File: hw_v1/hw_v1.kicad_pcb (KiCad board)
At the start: 4 copper layers, 116.5 x 98 mm, 234 parts, among them J10 Conn_01x01, J11 Conn_01x01, J12 Delphi_Sicma_24, J13 Delphi_Sicma_24, J14 Conn_01x04, J2 Conn_01x05, J3 Conn_01x05, J4 Conn_01x05, J5 Conn_01x03, J6 Conn_01x04, J8 USB_B, J9 Tag connect, Q1 AO3400A, Q2 AO3400A, Q3 FDS6890A, Q5 SS8050, Q6 AO3400A, SW2 SW_Push, U1 MCZ33810EK, U10 BMP280, U11 L78M05ABDT-TR, U12 LM74800, U13 STM32F407VGTx, U14 TJA1051T-3, U15 25LCxxx, U16 REF3033, U17 SRV05-4, U18 VNLD5090, U19 L78M05ABDT-TR, U2 TC4424A, U21 ADXL343, U3 TC4424A, U4 MAX9926UAEE+, U5 TPL7407LAPWR, U6 LMV324, U7 LMV324, U9 SP720ABTG, Y1 32.768kHz, Y2 25MHz

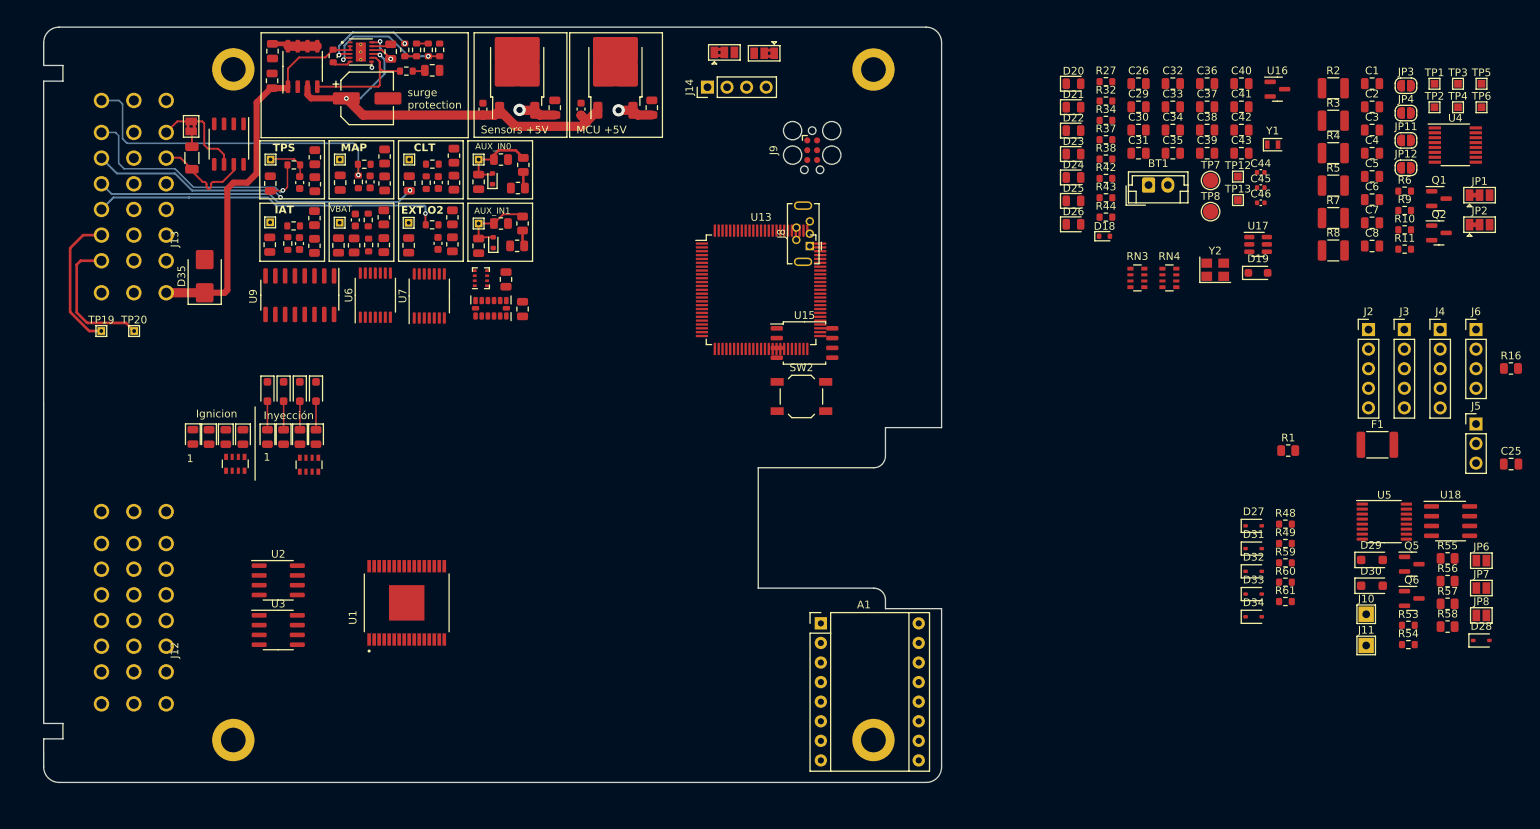
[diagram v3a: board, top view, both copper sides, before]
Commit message: placed al SMD, wip pmic traces
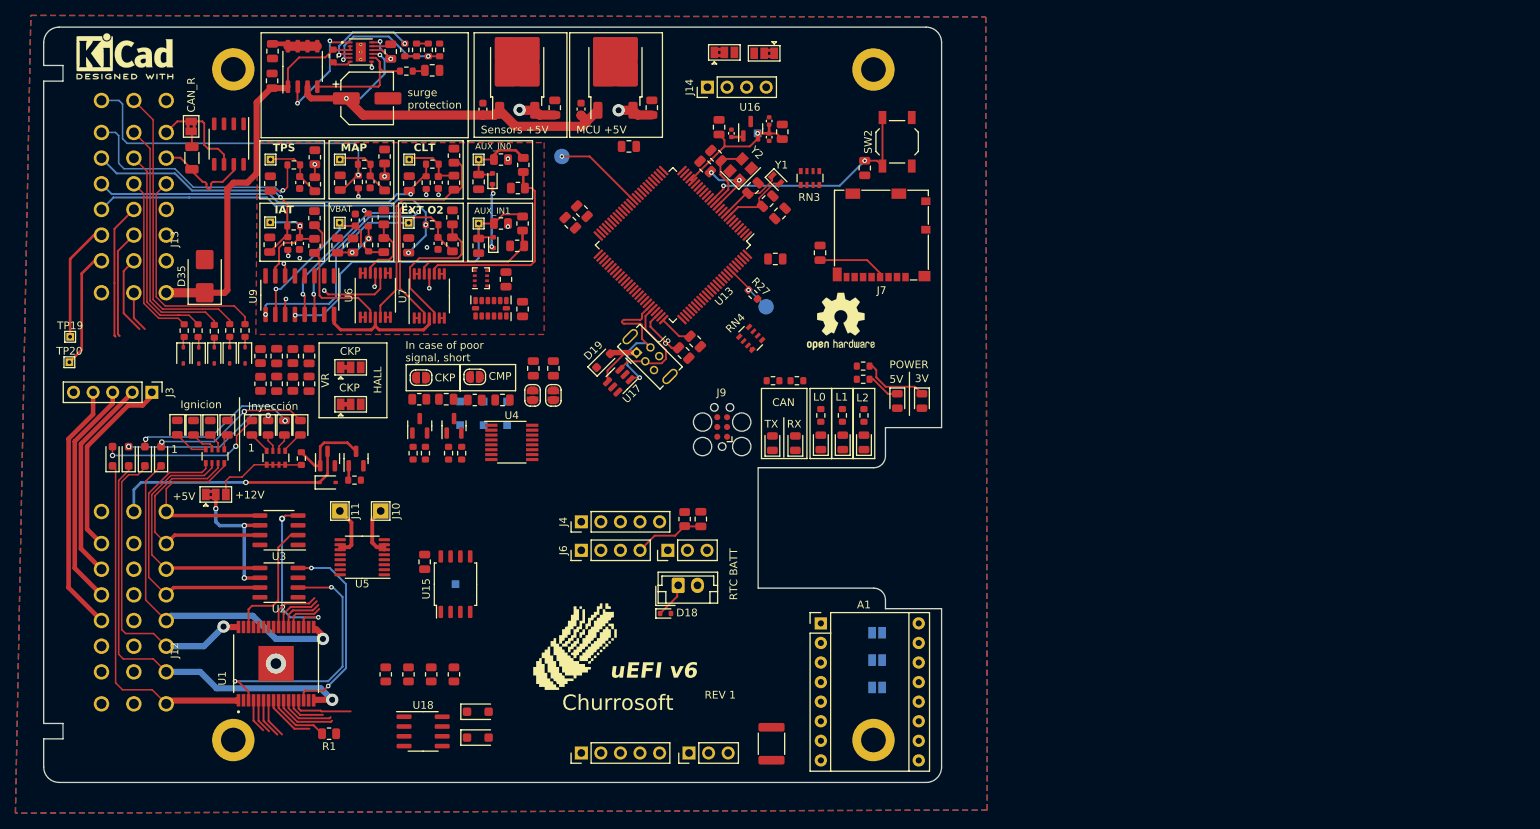
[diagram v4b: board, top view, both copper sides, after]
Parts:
- added Churrosoft: SYM_Hot_Large, OpenEFI-STM32F_rev3:churro_new_v4, F.Cu at (119.1, 133.7)
- added G***: LOGO, LOGO, B.Cu at (100.5, 102.0)
- added J15: Conn_01x03, Connector_PinHeader_2.54mm:PinHeader_1x03_P2.54mm_Vertical, F.Cu at (133.7, 147.5)
- added J7: 104031-0811, Connector_Card:microSD_HC_Molex_104031-0811, F.Cu at (158.7, 80.3)
- added JP13: Jumper_3_Bridged12, Jumper:SolderJumper-3_P1.3mm_Bridged2Bar12_Pad1.0x1.5mm, F.Cu at (72.3, 114.0)
- added LOGO1: Logo_Open_Hardware_Large, Symbol:OSHW-Logo2_9.8x8mm_SilkScreen, F.Cu at (153.4, 91.5)
- added SYM1: SYM_Hot_Small, Symbol:KiCad-Logo2_5mm_SilkScreen, F.Cu at (60.5, 57.1)
- JP6, JP7, JP8, TP1, TP12, TP13, TP2, TP3, TP4, TP5, TP6, TP7, TP8: moved to B.Cu
- R2, R3, R4, R5, R7, R8: footprint Resistor_SMD:R_1210_3225Metric -> Resistor_SMD:R_0805_2012Metric
- moved J3 162.7 mm to (64.0, 100.7), turned to -90 degrees
- moved D28 151.1 mm to (86.8, 112.4)
- moved JP2 148.3 mm to (89.8, 102.3)
- moved JP1 148.2 mm to (89.8, 97.5)
- moved C3 145.9 mm to (80.2, 99.6), turned to 90 degrees
- moved C2 145.8 mm to (80.2, 96.0), turned to -90 degrees
- moved R54 145.6 mm to (83.4, 109.3), turned to 90 degrees
- moved R49 145.5 mm to (68.2, 92.7), turned to 90 degrees
- moved R59 144.3 mm to (70.0, 92.7), turned to 90 degrees
- moved R2 143.5 mm to (78.1, 96.0), turned to -90 degrees
- moved C1 143.3 mm to (84.4, 99.6), turned to 90 degrees
- moved R60 142.7 mm to (72.1, 92.8), turned to 90 degrees
- moved Q6 141.8 mm to (86.8, 109.3), turned to 90 degrees
- moved R5 141.6 mm to (78.1, 99.6), turned to 90 degrees
- moved R61 141.4 mm to (74.1, 92.7), turned to 90 degrees
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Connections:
- A1 pad 15: /Relay & Power Outputs/MTR_STEP -> /MTR_STEP
- A1 pad 16: /Relay & Power Outputs/MTR_DIR -> /MTR_DIR
- A1 pad 2: /Relay & Power Outputs/MTR_FAULT -> /MTR_FAULT
- A1 pad 9: /Relay & Power Outputs/MTR_ENABLE -> /MTR_ENABLE
- C2 pad 1: CKP- -> CRANK-
- C3 pad 1: CMP- -> CAM-
- C7 pad 1: /CKP_CMP_Sensors/CKP -> /CKP
- C8 pad 1: /CKP_CMP_Sensors/CKP -> /CKP
- D27 pad 1: /Connector/SW_Clutch_m -> /SW_Clutch_m
- D31 pad 1: /Connector/SW_USER_m -> /SW_USER_m
- D32 pad 1: /Connector/SW_TABLE_m -> /SW_TABLE_m
- D33 pad 1: /Connector/SW_SHIFT_m -> /SW_SHIFT_m
- D34 pad 1: /Connector/SW_AC_m -> /SW_AC_m
- JP1 pad 2: CMP+ -> CAM+
- JP2 pad 2: CKP+ -> CRANK+
- Q1 pad 2: /CKP_CMP_Sensors/CMP -> /CMP
- Q2 pad 2: /CKP_CMP_Sensors/CKP -> /CKP
- R1 pad 2: /Injection & ignition drivers/PMIC1_ENABLE -> /PMIC1_ENABLE
- R10 pad 2: /CKP_CMP_Sensors/CMP -> /CMP
- R11 pad 2: /CKP_CMP_Sensors/CKP -> /CKP
- R2 pad 1: CKP- -> CRANK-
- R48 pad 1: /Connector/SW_Clutch_m -> /SW_Clutch_m
- R49 pad 1: /Connector/SW_USER_m -> /SW_USER_m
- R5 pad 1: CMP- -> CAM-
- R53 pad 1: /Relay & Power Outputs/RPM_OUT -> /RPM_OUT
- R55 pad 1: /Relay & Power Outputs/idle -> /idle
- R56 pad 2: /Relay & Power Outputs/boost -> /boost
- R57 pad 2: /Relay & Power Outputs/idle -> /idle
- R58 pad 2: /Relay & Power Outputs/boost -> /boost
- R59 pad 1: /Connector/SW_TABLE_m -> /SW_TABLE_m
- R6 pad 2: /CKP_CMP_Sensors/CMP -> /CMP
- R60 pad 1: /Connector/SW_SHIFT_m -> /SW_SHIFT_m
- R61 pad 1: /Connector/SW_AC_m -> /SW_AC_m
- R9 pad 2: /CKP_CMP_Sensors/CKP -> /CKP
- TP5 pad 1: /CKP_CMP_Sensors/CKP -> /CKP
- TP6 pad 1: /CKP_CMP_Sensors/CMP -> /CMP
- U1 pad 10: /Injection & ignition drivers/INY1 -> /INY1
- U1 pad 11: /Injection & ignition drivers/INY2 -> /INY2
- U1 pad 12: /Injection & ignition drivers/INY3 -> /INY3
- U1 pad 13: /Injection & ignition drivers/INY4 -> /INY4
- U1 pad 21: /Injection & ignition drivers/ECN4 -> /ECN3
- U1 pad 22: /Injection & ignition drivers/ECN3 -> /ECN4
- U1 pad 23: /Injection & ignition drivers/ECN2 -> /ECN1
- U1 pad 24: /Injection & ignition drivers/ECN1 -> /ECN2
- U1 pad 4: /Injection & ignition drivers/PMIC1_CS -> /PMIC1_CS
- U1 pad 5: /Injection & ignition drivers/SPI2_SCK -> /SPI2_SCK
- U1 pad 6: /Injection & ignition drivers/SPI2_MOSI -> /SPI2_MOSI
- U1 pad 7: /Injection & ignition drivers/SPI2_MISO -> /SPI2_MISO
- U1 pad 9: /Injection & ignition drivers/PMIC1_ENABLE -> /PMIC1_ENABLE
- U10 pad 2: /Sensors/BARO_CS -> /ACCL_CS
- U10 pad 3: /Sensors/SPI2_MOSI -> /SPI2_MOSI
- U10 pad 4: /Sensors/SPI2_SCK -> /SPI2_SCK
- U10 pad 5: /Sensors/SPI2_MISO -> /SPI2_MISO
- U13 pad 23: /TPS -> /IAT
- U13 pad 34: /BARO_CS -> /ACCL_CS
- U21 pad 12: /Sensors/SPI2_MISO -> /SPI2_MISO
- U21 pad 13: /Sensors/SPI2_MOSI -> /SPI2_MOSI
- U21 pad 14: /Sensors/SPI2_SCK -> /SPI2_SCK
- U21 pad 7: /Sensors/ACCL_CS -> /ACCL_CS
- U4 pad 4: /CKP_CMP_Sensors/CMP -> /CMP
- U4 pad 5: /CKP_CMP_Sensors/CKP -> /CKP
- U5 pad 1: /Relay & Power Outputs/fuel_pump -> /fuel_pump
- U5 pad 2: /Relay & Power Outputs/fan1 -> /fan1
- U5 pad 3: /Relay & Power Outputs/fan2 -> /fan2
- U5 pad 4: /Relay & Power Outputs/vvt -> /vvt
- U5 pad 5: /Relay & Power Outputs/vvt -> /vvt
- U6 pad 1: /Sensors/IAT -> /IAT
- U6 pad 13: /Sensors/VBATT -> VBATT
- U6 pad 14: /Sensors/VBATT -> VBATT
- U6 pad 2: /Sensors/IAT -> /IAT
- U6 pad 6: /Sensors/CLT -> /CLT
- U6 pad 7: /Sensors/CLT -> /CLT
- U6 pad 8: /Sensors/TPS -> /TPS
- U6 pad 9: /Sensors/TPS -> /TPS
- U7 pad 1: /Sensors/MAP -> /MAP
- U7 pad 2: /Sensors/MAP -> /MAP
- U7 pad 6: /Sensors/O2 -> /O2
- U7 pad 7: /Sensors/O2 -> /O2
- U9 pad 1: /Sensors/AUX_CH5_m -> unconnected-(U9-I1-Pad1)
- U9 pad 12: /Sensors/AUX_CH6_m -> ext_a0_in
- U9 pad 13: /Sensors/AUX_CH8_m -> ext_a1_in
- U9 pad 2: /Sensors/AUX_CH3_m -> unconnected-(U9-I2-Pad2)
- U9 pad 3: /Sensors/AUX_CH2_m -> unconnected-(U9-I3-Pad3)
- U9 pad 4: /Sensors/AUX_CH1_m -> unconnected-(U9-I4-Pad4)
- U9 pad 5: /Sensors/AUX_CH4_m -> unconnected-(U9-I5-Pad5)
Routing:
- net +5C: track 4.85 -> 78.8 mm, vias 1 -> 6
- net INJ-2-OUT: track 0.00 -> 57.4 mm, vias 0 -> 1
- net INJ-4-OUT: track 0.00 -> 45.5 mm, vias 0 -> 1
- net INJ-1-OUT: track 0.00 -> 45.4 mm
- net INJ-3-OUT: track 0.00 -> 40.1 mm, vias 0 -> 1
- net PROTO-5: track 0.00 -> 40.0 mm
- net SW_AC: track 0.00 -> 38.4 mm
- net ext_a1_in: track 10.9 -> 48.9 mm, vias 0 -> 2
- net /Sensors/CH_CLT_m: track 0.00 -> 37.6 mm, vias 0 -> 2
- net +3V3: track 0.00 -> 36.7 mm
- net /Sensors/CH_O2_m: track 0.00 -> 36.2 mm, vias 0 -> 1
- net IGN-1-OUT: track 0.00 -> 36.1 mm
- net /Sensors/CH_MAP_m: track 0.00 -> 34.7 mm, vias 0 -> 1
- net Net-(U1-GD0): track 0.00 -> 33.5 mm, vias 0 -> 2
- net ext_a0_in: track 10.2 -> 43.5 mm, vias 0 -> 1
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- added copper zone on B.Cu, net GND
- added copper zone on F.Cu, net GND
- added copper zone on In1.Cu, net GND
- added copper zone on In2.Cu, net GND
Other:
- board text added: "+12V"
- board text added: "+5V"
- board text added: "3V"
- board text added: "5V"
- board text added: "CAN"
- board text added: "CAN_R"
- board text added: "CKP"
- board text added: "CMP"
- board text added: "HALL"
- board text added: "In case of poor signal, short"
- board text added: "L0"
- board text added: "L1"
- board text added: "L2"
- board text added: "POWER"
- board text added: "REV 1"
- board text added: "RTC BATT"
- board text added: "RX"
- board text added: "TX"
- board text added: "VR"
- board text added: "uEFI v6"

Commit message: ckp/cmp sensor layout
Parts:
- removed LOGO1: Logo_Open_Hardware_Large, Symbol:OSHW-Logo2_9.8x8mm_SilkScreen
- removed SYM1: SYM_Hot_Small, Symbol:KiCad-Logo2_5mm_SilkScreen
- moved TP1 32.5 mm to (78.1, 96.2)
- moved RN3 12.3 mm to (149.8, 85.2)
- moved TP5 5.57 mm to (106.0, 107.1)
- moved JP10 5.25 mm to (138.2, 56.8)
- moved JP9 4.82 mm to (143.1, 56.9)
- moved TP6 3.65 mm to (100.5, 106.0)
- moved TP3 3.65 mm to (105.3, 98.7)
- moved TP2 1.90 mm to (111.2, 103.4)
- moved TP4 1.47 mm to (106.8, 103.5)
- moved C35 0.90 mm to (150.7, 81.7)
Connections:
- J12 pad B7: FUELPUMP-OUT -> VVT-OUT
- J12 pad C2: VVT-OUT -> IDLE-OUT
- J12 pad C3: IDLE-OUT -> FUELPUMP-OUT
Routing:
- net /CAN1_RX: track 0.00 -> 83.0 mm, vias 0 -> 2
- net /CAN1_TX: track 0.00 -> 79.8 mm, vias 0 -> 2
- net /CKP_CMP_Sensors/IN1-: track 0.00 -> 47.8 mm, vias 0 -> 2
- net /CKP_CMP_Sensors/IN1+: track 0.00 -> 43.6 mm, vias 0 -> 3
- net /CKP_CMP_Sensors/IN2-: track 0.00 -> 43.1 mm, vias 0 -> 4
- net CRANK+: track 14.5 -> 53.0 mm
- net /CKP_CMP_Sensors/IN2+: track 0.00 -> 38.4 mm, vias 0 -> 3
- net FUELPUMP-OUT: track 0.00 -> 37.1 mm, vias 0 -> 1
- net CAM+: track 5.31 -> 36.2 mm
- net VVT-OUT: track 0.00 -> 29.3 mm, vias 0 -> 1
- net FAN-OUT: track 0.00 -> 28.9 mm, vias 0 -> 1
- net +12V: track 81.8 -> 110.0 mm, vias 3 -> 4
- net FAN2-OUT: track 0.00 -> 28.0 mm, vias 0 -> 1
- net CAM-: track 10.3 -> 35.9 mm
- net CRANK-: track 17.6 -> 42.3 mm, vias 0 -> 2
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
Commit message: finish pcb layout
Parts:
- added C9: 100nF, Capacitor_SMD:C_0805_2012Metric, F.Cu at (134.1, 64.2)
- added U8: AMS1117-3.3, Package_TO_SOT_SMD:SOT-223-3_TabPin2, F.Cu at (135.1, 58.6)
- moved D18 66.4 mm to (153.9, 67.2), turned to -90 degrees
- moved BT1 60.6 mm to (150.4, 67.9), turned to 90 degrees
- moved JP10 48.9 mm to (124.6, 103.8)
- moved JP9 48.9 mm to (129.5, 103.8)
- moved J14 48.9 mm to (122.5, 108.1)
- moved F1 30.4 mm to (114.0, 147.2), turned to 0 degrees
- moved D30 15.2 mm to (95.8, 134.5), turned to -90 degrees
- moved D29 13.9 mm to (93.4, 137.1), turned to -90 degrees
- moved TP12 12.2 mm to (105.3, 113.5), turned to 0 degrees
- moved U15 12.2 mm to (105.3, 113.5), turned to 180 degrees
- moved R56 9.16 mm to (104.7, 131.9), turned to -90 degrees
- moved U18 8.14 mm to (101.1, 136.8), turned to 180 degrees
- moved R55 6.81 mm to (98.5, 131.9)
- moved C37 6.00 mm to (102.4, 117.5), turned to 0 degrees
- moved J4 5.58 mm to (122.3, 112.5)
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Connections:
- A1 pad 3: STEP-A2 -> STEPPER-A2
- A1 pad 4: STEP-A1 -> STEPPER-A1
- A1 pad 5: STEP-B1 -> STEPPER-B1
- A1 pad 6: STEP-B2 -> STEPPER-B2
- BT1 pad 1: VBATT -> Net-(BT1-+)
- C25 pad 2: MCU-D20 -> MCU-D0
- D18 pad 1: VBATT -> Net-(BT1-+)
- D29 pad 1: 12V-SW -> +12V
- D30 pad 1: 12V-SW -> +12V
- F1 pad 1: +3V3 -> +5C
- J6 pad 3: MCU-D21 -> MCU-D1
- J6 pad 4: MCU-D20 -> MCU-D0
- R16 pad 1: MCU-D20 -> MCU-D0
- RN3 pad 2: /SD_DAT1 -> /SD_CLK
- RN3 pad 4: /SD_CLK -> /SD_DAT1
- U10 pad 2: /ACCL_CS -> BARO_CS
- U13 pad 24: VBATT -> /VBATT
- U13 pad 34: /ACCL_CS -> BARO_CS
- U13 pad 35: unconnected-(U13-PB0-Pad35) -> MCU-D0
- U13 pad 36: unconnected-(U13-PB1-Pad36) -> MCU-D1
- U13 pad 6: VBATT -> Net-(BT1-+)
- U13 pad 95: /ACCL_CS -> ACCL_CS
- U21 pad 7: /ACCL_CS -> ACCL_CS
- U6 pad 13: VBATT -> /VBATT
- U6 pad 14: VBATT -> /VBATT
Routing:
- net +3V3: track 56.8 -> 484.1 mm, vias 0 -> 19
- net +5V: track 8.02 -> 248.7 mm, vias 2 -> 6
- net +12V: track 110.0 -> 341.1 mm, vias 4 -> 7
- net /SPI2_MISO: track 5.16 -> 177.2 mm, vias 0 -> 3
- net /SPI2_SCK: track 4.59 -> 174.4 mm, vias 0 -> 4
- net /SPI2_MOSI: track 5.19 -> 170.7 mm, vias 0 -> 4
- net /MTR_ENABLE: track 0.00 -> 113.0 mm, vias 0 -> 1
- net /MTR_STEP: track 0.00 -> 106.4 mm, vias 0 -> 1
- net /MTR_DIR: track 0.00 -> 106.1 mm, vias 0 -> 1
- net /PMIC1_CS: track 4.41 -> 107.1 mm, vias 0 -> 2
- net STEPPER-A2: track 0.00 -> 96.1 mm, vias 0 -> 1
- net +5C: track 78.8 -> 174.3 mm, vias 6 -> 8
- net STEPPER-A1: track 0.00 -> 94.3 mm, vias 0 -> 1
- net STEPPER-B2: track 0.00 -> 93.7 mm, vias 0 -> 1
- net /MTR_FAULT: track 0.00 -> 93.2 mm, vias 0 -> 1
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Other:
- board text added: "BT"
